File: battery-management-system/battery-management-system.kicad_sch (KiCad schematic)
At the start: 1 part

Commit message: add gitignore
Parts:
- gave numbers to parts that had none: 1
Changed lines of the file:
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@@
   (symbol (lib_id "benediktibk:STM32L071CZTx") (at 121.92 80.01 0) (unit 1)
     (in_bom yes) (on_board yes) (fields_autoplaced)
-    (property "Reference" "U?" (id 0) (at 126.4794 118.11 0)
+    (property "Reference" "U1" (id 0) (at 126.4794 118.11 0)
       (effects (font (size 1.27 1.27)) (justify left))
     )
@@
   (symbol_instances
     (path "/109ac41c-956a-4ddf-a748-ca748d1d9cf6"
-      (reference "U?") (unit 1) (value "STM32L071CZTx") (footprint "Package_QFP:LQFP-48_7x7mm_P0.5mm")
+      (reference "U1") (unit 1) (value "STM32L071CZTx") (footprint "Package_QFP:LQFP-48_7x7mm_P0.5mm")
     )
   )

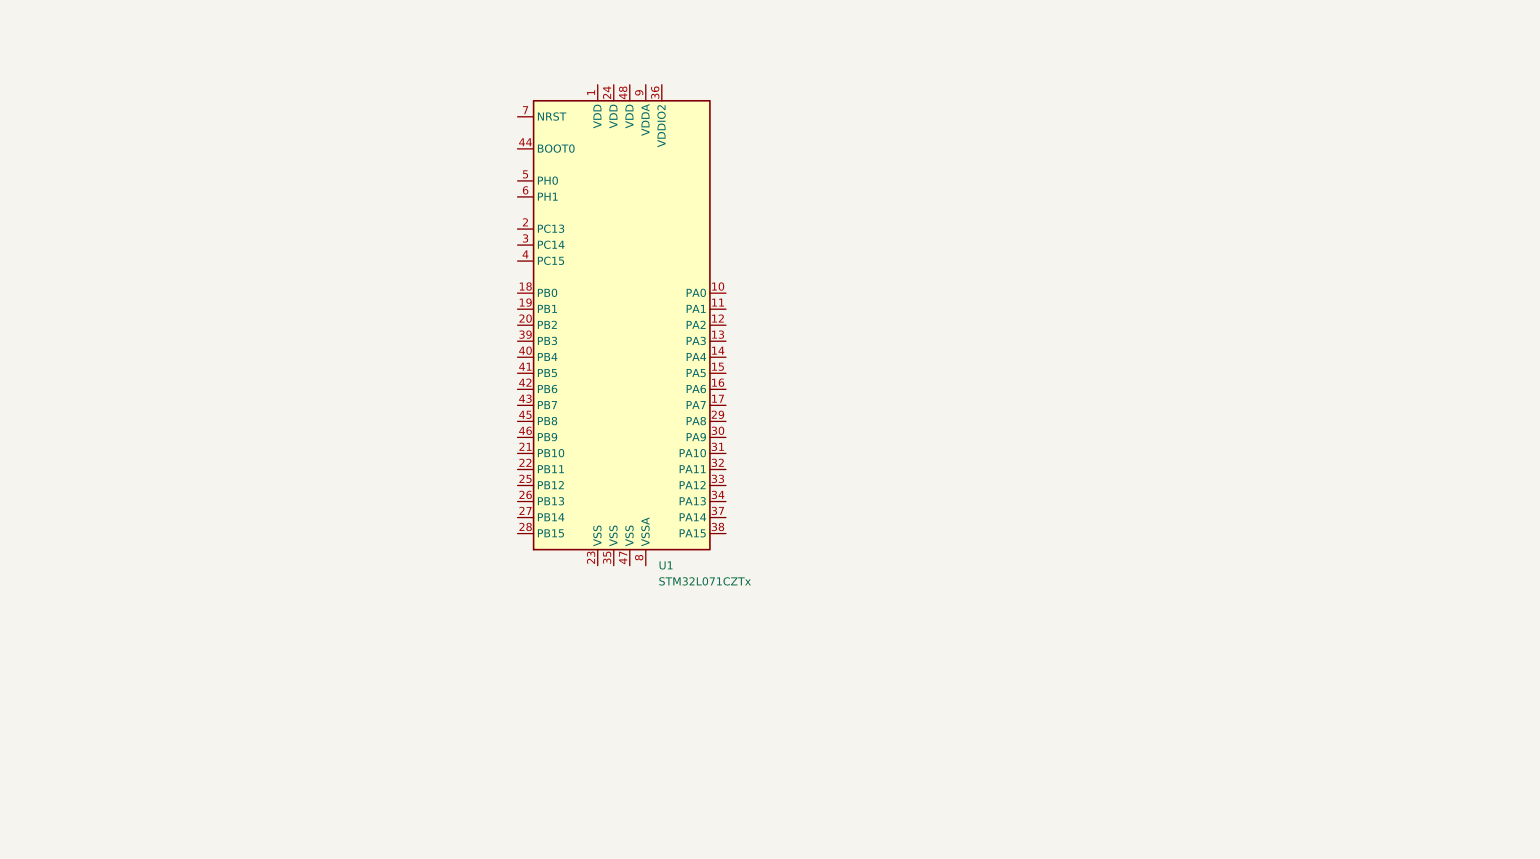
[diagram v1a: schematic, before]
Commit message: add USB and debug connectors
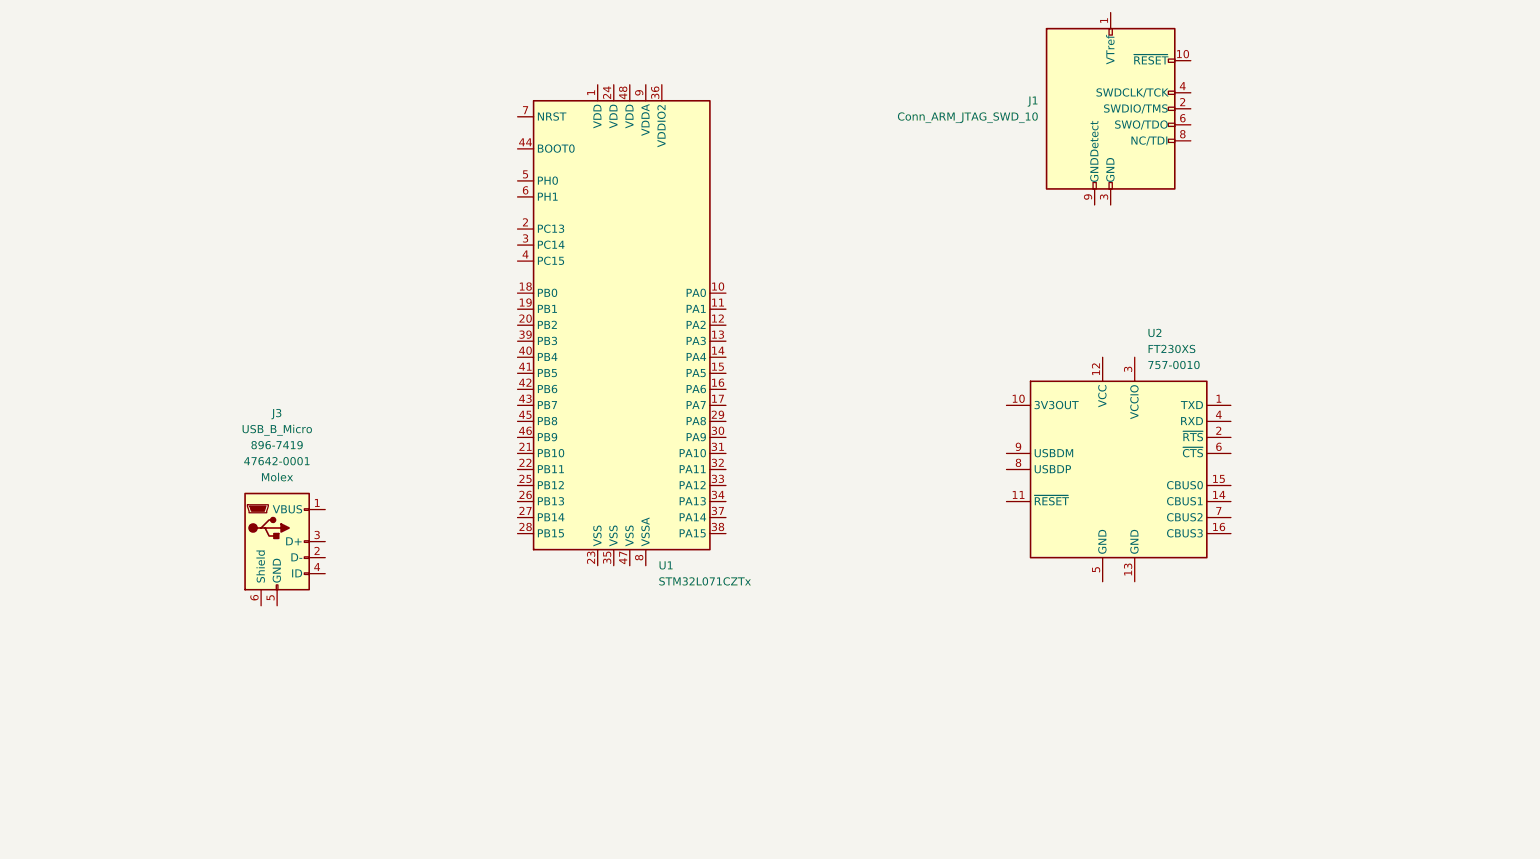
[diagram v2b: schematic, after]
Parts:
- added J1: Conn_ARM_JTAG_SWD_10, symbol benediktibk:Conn_ARM_JTAG_SWD_10
- added J3: USB_B_Micro, symbol benediktibk:USB_B_Micro
- added U2: FT230XS, Package_SO:SSOP-16_3.9x4.9mm_P0.635mm, symbol benediktibk:FT230XS
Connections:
- new net: J1.3 (GND), J1.5 (GND)
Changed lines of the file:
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@@
+    (pin "9")
+  )
+  (symbol (lib_id "benediktibk:FT230XS") (at 199.39 102.87 0) (unit 1)
+    (in_bom yes) (on_board yes) (fields_autoplaced)
+    (property "Reference" "U2" (id 0) (at 203.9494 81.28 0)
+      (effects (font (size 1.27 1.27)) (justify left))
+    )
+    (property "Value" "FT230XS" (id 1) (at 203.9494 83.82 0)
+      (effects (font (size 1.27 1.27)) (justify left))
+    )
+    (property "Footprint" "Package_SO:SSOP-16_3.9x4.9mm_P0.635mm" (id 2) (at 224.79 118.11 0)
+      (effects (font (size 1.27 1.27)) hide)
+    )
+    (property "Datasheet" "https://www.ftdichip.com/Support/Documents/DataSheets/ICs/DS_FT230X.pdf" (id 3) (at 199.39 102.87 0)
+      (effects (font (size 1.27 1.27)) hide)
+    )
+    (property "Order number RS-Online" "757-0010" (id 4) (at 203.9494 86.36 0)
+      (effects (font (size 1.27 1.27)) (justify left))
+    )
+    (pin "1")
+    (pin "10")
+    (pin "11")
+    (pin "12")
+    (pin "13")
+    (pin "14")
+    (pin "15")
+    (pin "16")
+    (pin "2")
+    (pin "3")
+    (pin "4")
+    (pin "5")
+    (pin "6")
+    (pin "7")
+    (pin "8")
+    (pin "9")
+  )
+  (symbol (lib_id "benediktibk:USB_B_Micro") (at 66.04 114.3 0) (unit 1)
+    (in_bom yes) (on_board yes) (fields_autoplaced)
+    (property "Reference" "J3" (id 0) (at 66.04 93.98 0))
+    (property "Value" "USB_B_Micro" (id 1) (at 66.04 96.52 0))
+    (property "Footprint" "" (id 2) (at 69.85 115.57 0)
+      (effects (font (size 1.27 1.27)) hide)
+    )
+    (property "Datasheet" "~" (id 3) (at 69.85 115.57 0)
+      (effects (font (size 1.27 1.27)) hide)
+    )
+    (property "Order Number RS-Online" "    896-7419" (id 4) (at 66.04 99.06 0))
+    (property "Part Number" "    47642-0001" (id 5) (at 66.04 101.6 0))
+    (property "Manufacturer" "Molex" (id 6) (at 66.04 104.14 0))
+    (pin "1")
+    (pin "2")
+    (pin "3")
+    (pin "4")
+    (pin "5")
+    (pin "6")
+  )
+  (symbol (lib_id "benediktibk:Conn_ARM_JTAG_SWD_10") (at 198.12 45.72 0) (unit 1)
+    (in_bom yes) (on_board yes) (fields_autoplaced)
+    (property "Reference" "J1" (id 0) (at 186.69 44.4499 0)
+      (effects (font (size 1.27 1.27)) (justify right))
+    )
+    (property "Value" "Conn_ARM_JTAG_SWD_10" (id 1) (at 186.69 46.9899 0)
+      (effects (font (size 1.27 1.27)) (justify right))
+    )
+    (property "Footprint" "" (id 2) (at 198.12 45.72 0)
+      (effects (font (size 1.27 1.27)) hide)
+    )
+    (property "Datasheet" "http://infocenter.arm.com/help/topic/com.arm.doc.ddi0314h/DDI0314H_coresight_components_trm.pdf" (id 3) (at 189.23 77.47 90)
+      (effects (font (size 1.27 1.27)) hide)
+    )
+    (pin "1")
+    (pin "10")
+    (pin "2")
+    (pin "3")
+    (pin "4")
+    (pin "5")
+    (pin "6")
+    (pin "7")
+    (pin "8")
     (pin "9")
   )
@@
   )
   (symbol_instances
+    (path "/f2f18fb0-92de-4b9e-be9f-6887f05d737c"
+      (reference "J1") (unit 1) (value "Conn_ARM_JTAG_SWD_10") (footprint "")
+    )
+    (path "/d85729e6-9484-434c-ab8a-ed3a9c7d0f24"
+      (reference "J3") (unit 1) (value "USB_B_Micro") (footprint "")
+    )
     (path "/109ac41c-956a-4ddf-a748-ca748d1d9cf6"
       (reference "U1") (unit 1) (value "STM32L071CZTx") (footprint "Package_QFP:LQFP-48_7x7mm_P0.5mm")
     )
+    (path "/7b5c54ea-3a3d-4776-944d-547ce13e0271"
+      (reference "U2") (unit 1) (value "FT230XS") (footprint "Package_SO:SSOP-16_3.9x4.9mm_P0.635mm")
+    )
   )

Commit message: add charge and discharge FETs
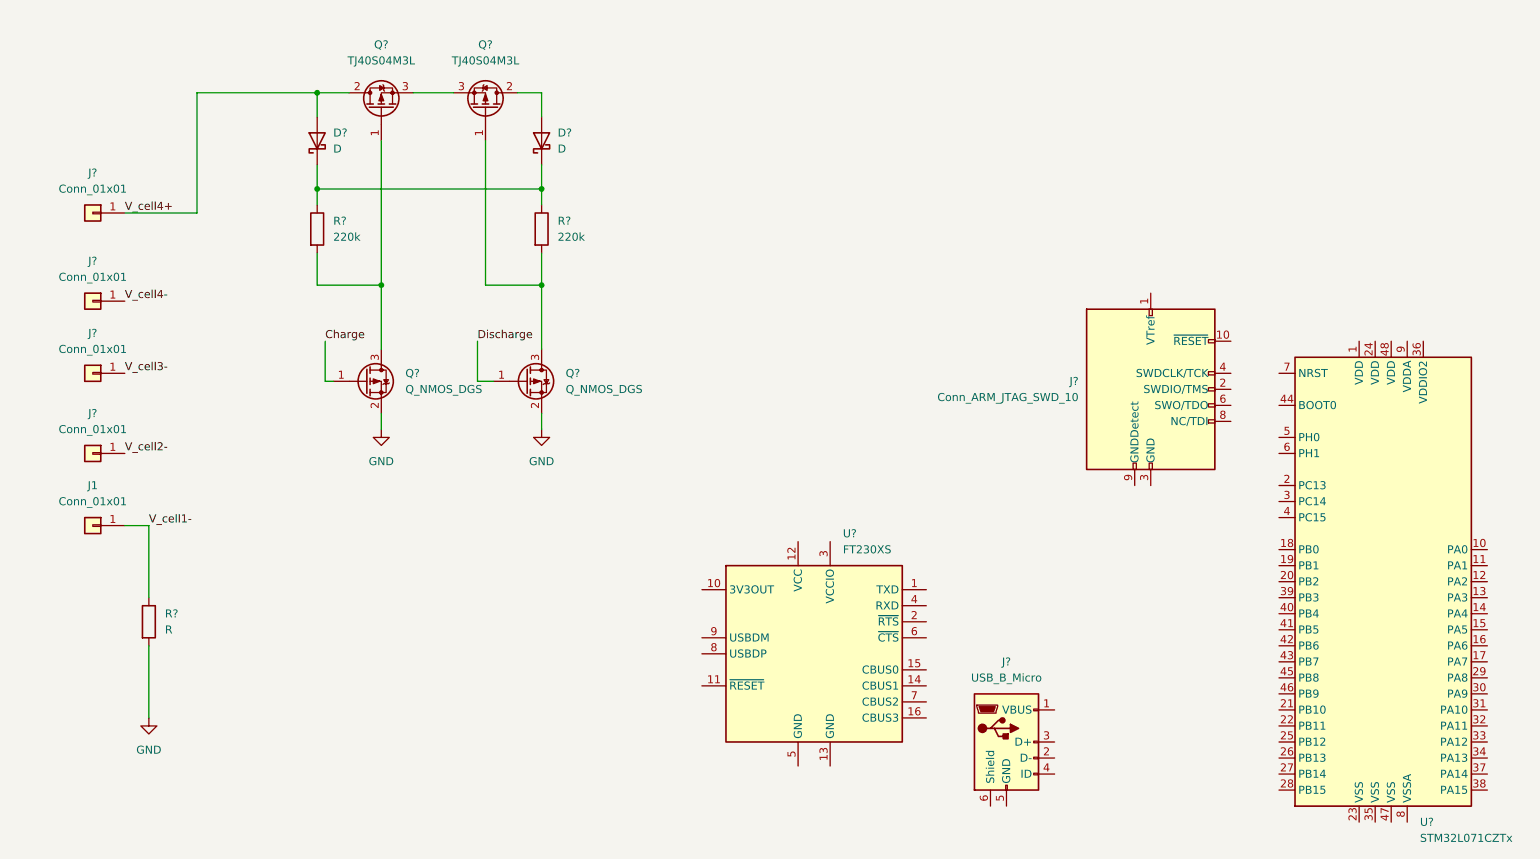
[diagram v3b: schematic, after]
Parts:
- removed J1: Conn_ARM_JTAG_SWD_10, symbol benediktibk:Conn_ARM_JTAG_SWD_10
- removed J3: USB_B_Micro, symbol benediktibk:USB_B_Micro
- removed U1: STM32L071CZTx, Package_QFP:LQFP-48_7x7mm_P0.5mm, symbol benediktibk:STM32L071CZTx
- removed U2: FT230XS, Package_SO:SSOP-16_3.9x4.9mm_P0.635mm, symbol benediktibk:FT230XS
- added D? (x2): D, Diode_SMD:D_SOD-323, symbol Device:D_Schottky
- added J1, J? (x4): Conn_01x01, symbol Connector_Generic:Conn_01x01
- added J?: USB_B_Micro, symbol Connector:USB_B_Micro
- added J?: Conn_ARM_JTAG_SWD_10, symbol Connector:Conn_ARM_JTAG_SWD_10
- added Q? (x2): Q_NMOS_DGS, Package_TO_SOT_SMD:SOT-23, symbol benediktibk:DMN3730U
- added Q? (x2): TJ40S04M3L, Package_TO_SOT_SMD:TO-252-2, symbol benediktibk:TJ40S04M3L
- added R? (x2): 220k, Resistor_SMD:R_0603_1608Metric, symbol Device:R
- added R?: R, symbol Device:R
- added U?: STM32L071CZTx, Package_QFP:LQFP-48_7x7mm_P0.5mm, symbol MCU_ST_STM32L0:STM32L071CZTx
- added U?: FT230XS, Package_SO:SSOP-16_3.9x4.9mm_P0.635mm, symbol Interface_USB:FT230XS
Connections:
- new net: Q?.1 (G), Q?.3 (D), R?.2 (x2)
- new net: D?.1 (K), D?.1 (K), R?.1, R?.1
- new net: D?.2 (A), Q?.2 (D)
- new net: Q?.3 (S), Q?.3 (S)
- new net: J?.3 (GND), J?.5 (GND)
- new net Charge: Q?.1 (G)
- new net Discharge: Q?.1 (G)
- new net GND: Q?.2 (S), Q?.2 (S), R?.2
- new net V_cell1-: J1.1 (Pin_1), R?.1
- new net V_cell2-: J?.1 (Pin_1)
- new net V_cell3-: J?.1 (Pin_1)
- new net V_cell4+: D?.2 (A), J?.1 (Pin_1), Q?.2 (D)
- new net V_cell4-: J?.1 (Pin_1)

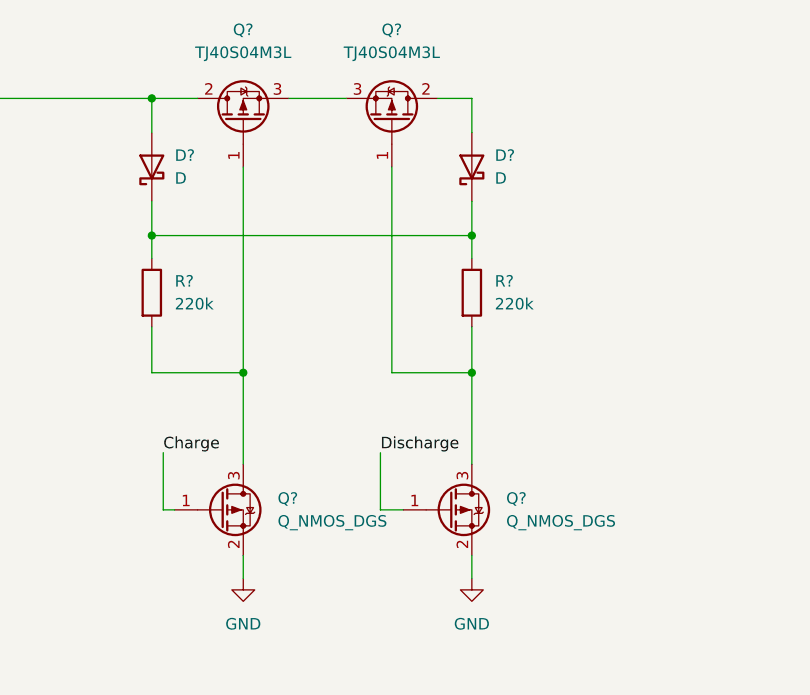
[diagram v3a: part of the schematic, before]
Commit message: select diode for charge and discharge FETs
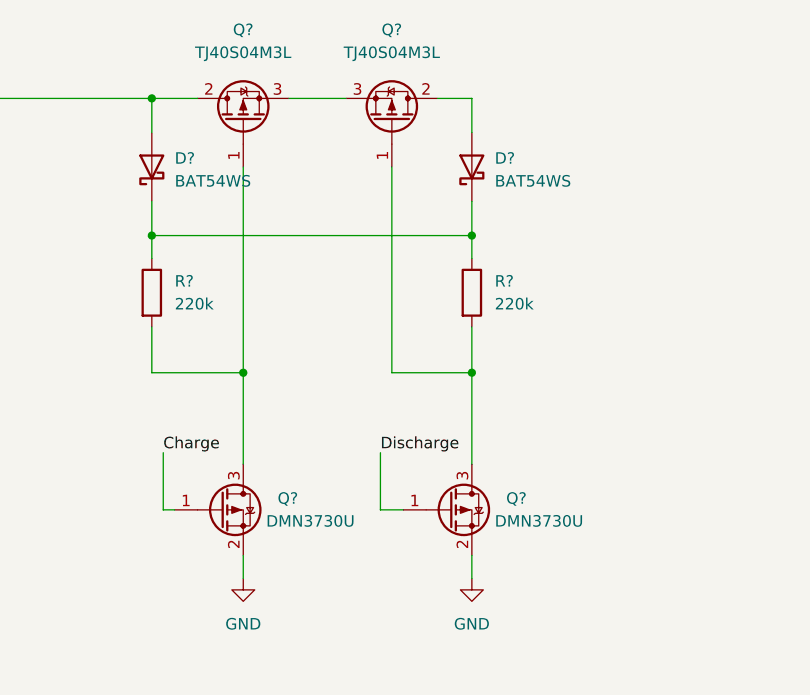
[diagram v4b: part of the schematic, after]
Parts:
- removed D? (x2): D, Diode_SMD:D_SOD-323, symbol Device:D_Schottky
- added D? (x2): BAT54WS, Diode_SMD:D_SOD-323, symbol benediktibk:BAT54WS
- Q? (x2): value Q_NMOS_DGS -> DMN3730U
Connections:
- net V_cell4+: now also D?.2 (A)
- net at R?.1, R?.1: now also D?.1 (K), D?.1 (K)
- net at Q?.2 (D): now also D?.2 (A)
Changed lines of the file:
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@@
       (effects (font (size 1.27 1.27)) (justify left))
     )
-    (property "Value" "Q_NMOS_DGS" (id 1) (at 111.76 90.1699 0)
+    (property "Value" "DMN3730U" (id 1) (at 110.49 90.17 0)
       (effects (font (size 1.27 1.27)) (justify left))
     )
@@
     (pin "2")
     (pin "3")
-  )
-  (symbol (lib_id "Device:D_Schottky") (at 107.95 50.8 90) (unit 1)
-    (in_bom yes) (on_board yes) (fields_autoplaced)
-    (property "Reference" "D?" (id 0) (at 110.49 49.5299 90)
-      (effects (font (size 1.27 1.27)) (justify right))
-    )
-    (property "Value" "D" (id 1) (at 110.49 52.0699 90)
-      (effects (font (size 1.27 1.27)) (justify right))
-    )
-    (property "Footprint" "Diode_SMD:D_SOD-323" (id 2) (at 107.95 50.8 0)
-      (effects (font (size 1.27 1.27)) hide)
-    )
-    (property "Datasheet" "~" (id 3) (at 107.95 50.8 0)
-      (effects (font (size 1.27 1.27)) hide)
-    )
-    (pin "1")
-    (pin "2")
   )
   (symbol (lib_id "Connector_Generic:Conn_01x01") (at 36.83 100.33 0) (mirror y) (unit 1)
@@
     )
     (property "Datasheet" "~" (id 3) (at 45.72 127 0)
+      (effects (font (size 1.27 1.27)) hide)
+    )
+    (pin "1")
+    (pin "2")
+  )
+  (symbol (lib_id "benediktibk:BAT54WS") (at 72.39 50.8 90) (unit 1)
+    (in_bom yes) (on_board yes) (fields_autoplaced)
+    (property "Reference" "D?" (id 0) (at 74.93 49.8474 90)
+      (effects (font (size 1.27 1.27)) (justify right))
+    )
+    (property "Value" "BAT54WS" (id 1) (at 74.93 52.3874 90)
+      (effects (font (size 1.27 1.27)) (justify right))
+    )
+    (property "Footprint" "Diode_SMD:D_SOD-323" (id 2) (at 72.39 50.8 0)
+      (effects (font (size 1.27 1.27)) hide)
+    )
+    (property "Datasheet" "~" (id 3) (at 72.39 50.8 0)
       (effects (font (size 1.27 1.27)) hide)
     )
@@
     (pin "2")
   )
-  (symbol (lib_id "benediktibk:DMN3730U") (at 80.01 88.9 0) (unit 1)
+  (symbol (lib_name "DMN3730U_1") (lib_id "benediktibk:DMN3730U") (at 80.01 88.9 0) (unit 1)
     (in_bom yes) (on_board yes) (fields_autoplaced)
     (property "Reference" "Q?" (id 0) (at 86.36 87.6299 0)
       (effects (font (size 1.27 1.27)) (justify left))
     )
-    (property "Value" "Q_NMOS_DGS" (id 1) (at 86.36 90.1699 0)
+    (property "Value" "DMN3730U" (id 1) (at 85.09 90.17 0)
       (effects (font (size 1.27 1.27)) (justify left))
     )
@@
     )
     (pin "1")
+  )
+  (symbol (lib_id "benediktibk:BAT54WS") (at 107.95 50.8 90) (unit 1)
+    (in_bom yes) (on_board yes) (fields_autoplaced)
+    (property "Reference" "D?" (id 0) (at 110.49 49.8474 90)
+      (effects (font (size 1.27 1.27)) (justify right))
+    )
+    (property "Value" "BAT54WS" (id 1) (at 110.49 52.3874 90)
+      (effects (font (size 1.27 1.27)) (justify right))
+    )
+    (property "Footprint" "Diode_SMD:D_SOD-323" (id 2) (at 107.95 50.8 0)
+      (effects (font (size 1.27 1.27)) hide)
+    )
+    (property "Datasheet" "~" (id 3) (at 107.95 50.8 0)
+      (effects (font (size 1.27 1.27)) hide)
+    )
+    (pin "1")
+    (pin "2")
   )
   (symbol (lib_id "Interface_USB:FT230XS") (at 151.13 132.08 0) (unit 1)
@@
     (pin "1")
   )
-  (symbol (lib_id "Device:D_Schottky") (at 72.39 50.8 90) (unit 1)
-    (in_bom yes) (on_board yes) (fields_autoplaced)
-    (property "Reference" "D?" (id 0) (at 74.93 49.5299 90)
-      (effects (font (size 1.27 1.27)) (justify right))
-    )
-    (property "Value" "D" (id 1) (at 74.93 52.0699 90)
-      (effects (font (size 1.27 1.27)) (justify right))
-    )
-    (property "Footprint" "Diode_SMD:D_SOD-323" (id 2) (at 72.39 50.8 0)
-      (effects (font (size 1.27 1.27)) hide)
-    )
-    (property "Datasheet" "~" (id 3) (at 72.39 50.8 0)
-      (effects (font (size 1.27 1.27)) hide)
-    )
-    (pin "1")
-    (pin "2")
-  )
   (sheet_instances
     (path "/" (page "1"))
@@
       (reference "#PWR?") (unit 1) (value "GND") (footprint "")
     )
-    (path "/4fa7fb95-77ab-4807-943e-cf077a8ac6e4"
-      (reference "D?") (unit 1) (value "D") (footprint "Diode_SMD:D_SOD-323")
-    )
-    (path "/f8b1fe1e-7171-413e-b564-701675427a84"
-      (reference "D?") (unit 1) (value "D") (footprint "Diode_SMD:D_SOD-323")
+    (path "/96b379fb-5fea-4df4-af17-f32f32a28ead"
+      (reference "D?") (unit 1) (value "BAT54WS") (footprint "Diode_SMD:D_SOD-323")
+    )
+    (path "/e9930cd2-204a-4ade-9278-24354b2bc364"
+      (reference "D?") (unit 1) (value "BAT54WS") (footprint "Diode_SMD:D_SOD-323")
     )
     (path "/08bc58d7-be94-486b-8c99-423f29316e45"
@@
     )
     (path "/3067b909-68e0-4976-8328-d5352d80a900"
-      (reference "Q?") (unit 1) (value "Q_NMOS_DGS") (footprint "Package_TO_SOT_SMD:SOT-23")
+      (reference "Q?") (unit 1) (value "DMN3730U") (footprint "Package_TO_SOT_SMD:SOT-23")
     )
     (path "/5988397e-c5d8-4a90-af2d-a94ce4b01b50"
@@
     )
     (path "/babdecc1-a0b4-4a48-82ce-6974bffbc3d0"
-      (reference "Q?") (unit 1) (value "Q_NMOS_DGS") (footprint "Package_TO_SOT_SMD:SOT-23")
+      (reference "Q?") (unit 1) (value "DMN3730U") (footprint "Package_TO_SOT_SMD:SOT-23")
     )
     (path "/6af9ff63-c55a-4ae0-ba45-db226c47684c"
